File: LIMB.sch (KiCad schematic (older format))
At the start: 67 parts, among them J2 MICROSD, J6 DEBUG, M1 FAN-4PIN, Q12 FK3303010L, Q13 FK3303010L, Q20 FK3303010L, Q21 FK3303010L, Q3 IRLML6402, U10 MAX3232PW, U11 NUF2042XV6, U12 NUF2042XV6, U13 NUF2042XV6, U14 NUF2042XV6, U15 2048mV, U9 NUF2042XV6

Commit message: Squiggles! Silk!
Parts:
- renumbered C134 to C201, C135 to C202, C136 to C203, C137 to C204, C131 to C205, C138 to C206, C139 to C207, C140 to C208, C141 to C209, C9 to C210, C130 to C211, C129 to C212, C127 to C213, C128 to C214, C125 to C215, C126 to C216, J6 to J201, J2 to J202, M1 to M201, Q3 to Q201, Q13 to Q202, Q21 to Q203, Q12 to Q204, Q20 to Q205, R131 to R201, R17 to R202, R102 to R203, R103 to R204, R104 to R205, R116 to R206, R139 to R207, R140 to R208, R142 to R209, R144 to R210, R141 to R211, R143 to R212, R56 to R213, R120 to R214, R121 to R215, R122 to R216, R123 to R217, R124 to R218, R125 to R219, R95 to R220, R126 to R221, R4 to R222, R94 to R223, R93 to R224, R92 to R225, R9 to R226, R86 to R227, R97 to R228, R3 to R229, R87 to R230, R8 to R231, R55 to R232, R96 to R233, U15 to U201, U12 to U202, U13 to U203, U14 to U204, U11 to U205, U10 to U206, U9 to U207, W6 to W201, W7 to W202

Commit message: Initial BOM
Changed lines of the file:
@@
 Wire Wire Line
 	5800 8700 5700 8700
+Wire Notes Line
+	2350 11000 2350 0
+Wire Notes Line
+	4350 0    4350 11000
+Wire Notes Line
+	6300 11000 6300 0
+Wire Notes Line
+	8300 0    8300 11000
+Wire Notes Line
+	10250 11000 10250 0
+Wire Notes Line
+	12200 0    12200 11000
+Wire Notes Line
+	14150 11000 14150 0
+Wire Notes Line
+	16150 0    16150 11000
+Wire Notes Line
+	0    2400 17000 2400
+Wire Notes Line
+	0    4350 17000 4350
+Wire Notes Line
+	17000 6300 -50  6300
+Wire Notes Line
+	0    8300 17000 8300
+Wire Notes Line
+	17000 10250 0    10250
 $EndSCHEMATC

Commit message: Final BOM
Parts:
- added R234: 51, IPC7351-Nominal:RESC1005X40, symbol R-0402
- C212: value 100n -> 1u; BOM CAP MLCC 100n ≥X5R 25V 10% [0402] -> CAP MLCC 1u 6.3V [0402]
- R201, R203, R204, R205, R206, R220, R229: value 5k1 -> 4k3; BOM RES SMD 5k1 1% [0402] -> RES SMD 4k3 [0402]
- R202: value 24 -> 51; BOM RES SMD 24 1% [0402] -> RES SMD 51 1% [0402]
- R207, R208, R210, R211, R212: value 5k1 -> 4k3; BOM RES SMD 5k1 1% [0402] -> RES SMD 4k3 1% [0402]
- R209: value 51k -> 22k6; BOM RES SMD 51k 1% [0402] -> RES SMD 22k6 1% [0402]
- R226, R227, R228, R231, R232, R233: value 3k9 -> 4k3; BOM RES SMD 3k9 1% [0402] -> RES SMD 4k3 1% [0402]
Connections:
- net FPGA_DATA: now also R234.2
- net MOSI: now also R234.1
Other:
- moved on the sheet: R202, R229

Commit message: Finish most redone routing
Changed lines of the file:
@@
 Wire Wire Line
 	5800 8700 5700 8700
-Wire Notes Line
-	2350 11000 2350 0
-Wire Notes Line
-	4350 0    4350 11000
-Wire Notes Line
-	6300 11000 6300 0
-Wire Notes Line
-	8300 0    8300 11000
-Wire Notes Line
-	10250 11000 10250 0
-Wire Notes Line
-	12200 0    12200 11000
-Wire Notes Line
-	14150 11000 14150 0
-Wire Notes Line
-	16150 0    16150 11000
-Wire Notes Line
-	0    2400 17000 2400
-Wire Notes Line
-	0    4350 17000 4350
-Wire Notes Line
-	17000 6300 -50  6300
-Wire Notes Line
-	0    8300 17000 8300
-Wire Notes Line
-	17000 10250 0    10250
 $Comp
 L R-0402 R234

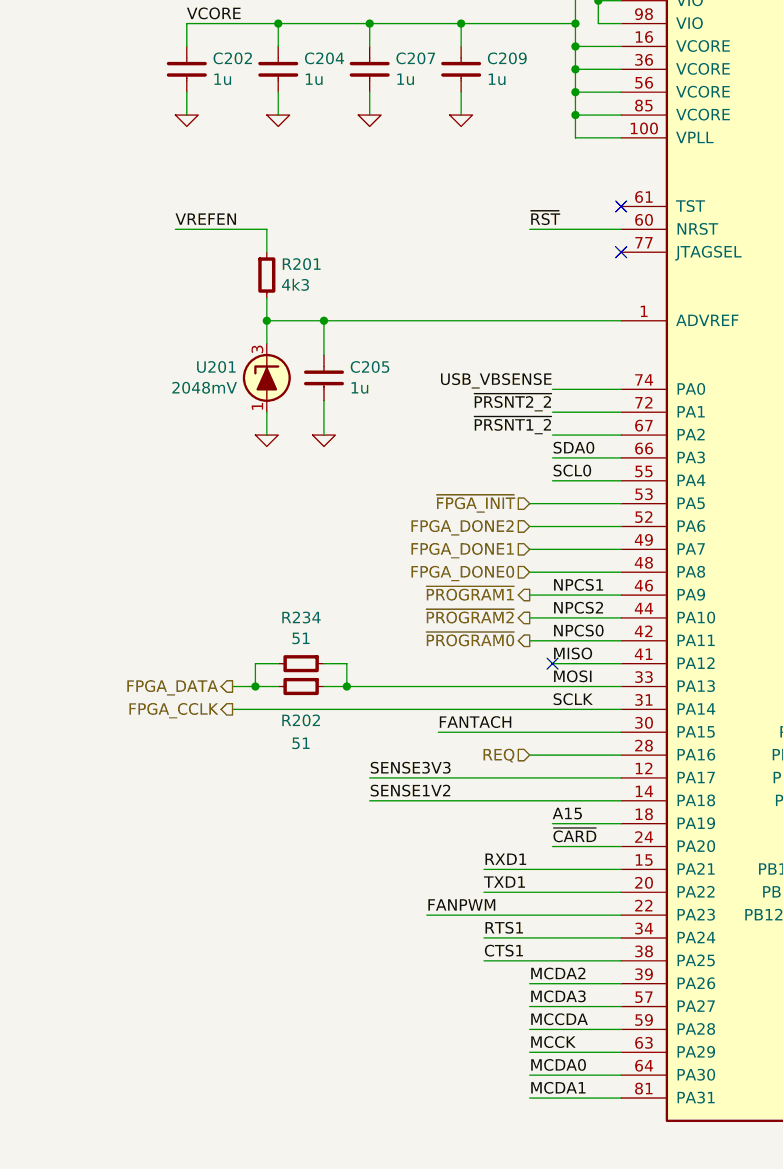
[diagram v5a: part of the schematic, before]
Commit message: Add some test points
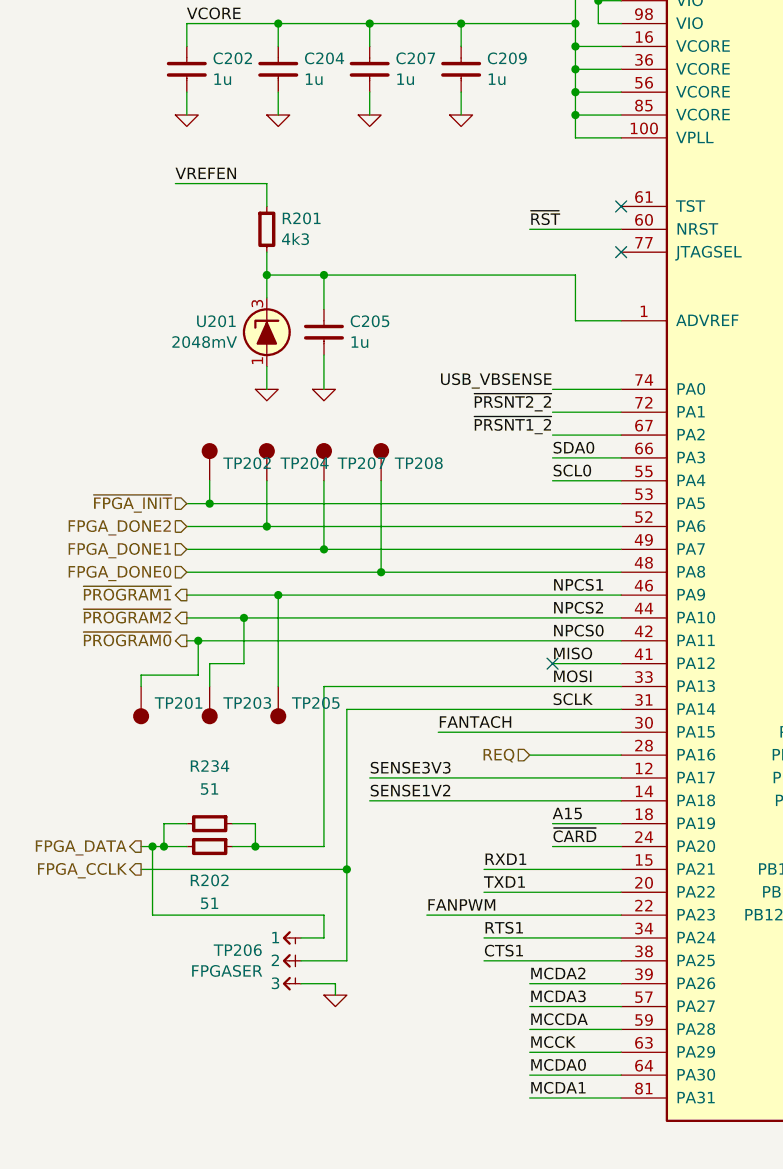
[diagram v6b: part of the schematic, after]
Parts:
- added TP201, TP202, TP203, TP204, TP205, TP207, TP208: TESTPOINT, conn-test:TEST-SMD-SMALL, symbol TESTPOINT
- added TP206: FPGASER, conn-100mil:CONN-100MIL-M-1x3, symbol CONN-100MIL-M-1x3
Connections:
- net FPGA_CCLK: now also TP206.2
- net FPGA_DATA: now also TP206.1
- net FPGA_DONE0: now also TP208.1
- net FPGA_DONE1: now also TP207.1
- net FPGA_DONE2: now also TP204.1
- net GND: now also TP206.3
- net ~FPGA_INIT: now also TP202.1
- net ~PROGRAM0: now also TP201.1
- net ~PROGRAM1: now also TP205.1
- net ~PROGRAM2: now also TP203.1
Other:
- moved on the sheet: C205, R201, R202, R234, U201

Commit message: Fix more shit for to pass ERC
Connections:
- net ~SDRAM_RST: now reaches LIMB1.93 (PB13)
- no-connect marks 14 -> 13
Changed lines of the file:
@@
 USB_D-
 $Comp
-L GND #PWR213
+L GND #PWR031
 U 1 1 577EAB82
 P 4400 6700
-F 0 "#PWR213" H 4400 6700 30  0001 C CNN
+F 0 "#PWR031" H 4400 6700 30  0001 C CNN
 F 1 "GND" H 4400 6630 30  0001 C CNN
 F 2 "" H 4400 6700 60  0000 C CNN
@@
 $EndComp
 $Comp
-L GND #PWR223
+L GND #PWR032
 U 1 1 577EDCE7
 P 10400 4700
-F 0 "#PWR223" H 10400 4700 30  0001 C CNN
+F 0 "#PWR032" H 10400 4700 30  0001 C CNN
 F 1 "GND" H 10400 4630 30  0001 C CNN
 F 2 "" H 10400 4700 60  0000 C CNN
@@
 MCDA3
 $Comp
-L GND #PWR222
+L GND #PWR033
 U 1 1 577EDF0A
 P 10400 4000
-F 0 "#PWR222" H 10400 4000 30  0001 C CNN
+F 0 "#PWR033" H 10400 4000 30  0001 C CNN
 F 1 "GND" H 10400 3930 30  0001 C CNN
 F 2 "" H 10400 4000 60  0000 C CNN
@@
 P3V3_CARD
 $Comp
-L GND #PWR220
+L GND #PWR034
 U 1 1 577EEC84
 P 9600 4200
-F 0 "#PWR220" H 9600 4200 30  0001 C CNN
+F 0 "#PWR034" H 9600 4200 30  0001 C CNN
 F 1 "GND" H 9600 4130 30  0001 C CNN
 F 2 "" H 9600 4200 60  0000 C CNN
@@
 ~RST
 $Comp
-L GND #PWR212
+L GND #PWR035
 U 1 1 579F6A32
 P 2800 8000
-F 0 "#PWR212" H 2800 8000 30  0001 C CNN
+F 0 "#PWR035" H 2800 8000 30  0001 C CNN
 F 1 "GND" H 2800 7930 30  0001 C CNN
 F 2 "" H 2800 8000 60  0000 C CNN
@@
 $EndComp
 $Comp
-L GND #PWR232
+L GND #PWR036
 U 1 1 57A172F2
 P 14800 1650
-F 0 "#PWR232" H 14800 1650 30  0001 C CNN
+F 0 "#PWR036" H 14800 1650 30  0001 C CNN
 F 1 "GND" H 14800 1580 30  0001 C CNN
 F 2 "" H 14800 1650 60  0000 C CNN
@@
 $EndComp
 $Comp
-L GND #PWR228
+L GND #PWR037
 U 1 1 57A1D8E5
 P 13950 3400
-F 0 "#PWR228" H 13950 3400 30  0001 C CNN
+F 0 "#PWR037" H 13950 3400 30  0001 C CNN
 F 1 "GND" H 13950 3330 30  0001 C CNN
 F 2 "" H 13950 3400 60  0000 C CNN
@@
 $EndComp
 $Comp
-L GND #PWR226
+L GND #PWR038
 U 1 1 57A1DE24
 P 12050 3400
-F 0 "#PWR226" H 12050 3400 30  0001 C CNN
+F 0 "#PWR038" H 12050 3400 30  0001 C CNN
 F 1 "GND" H 12050 3330 30  0001 C CNN
 F 2 "" H 12050 3400 60  0000 C CNN
@@
 $EndComp
 $Comp
-L GND #PWR225
+L GND #PWR039
 U 1 1 57A1E179
 P 11800 3250
-F 0 "#PWR225" H 11800 3250 30  0001 C CNN
+F 0 "#PWR039" H 11800 3250 30  0001 C CNN
 F 1 "GND" H 11800 3180 30  0001 C CNN
 F 2 "" H 11800 3250 60  0000 C CNN
@@
 P3V3_STBY
 $Comp
-L GND #PWR227
+L GND #PWR040
 U 1 1 57A1EEA9
 P 12300 4200
-F 0 "#PWR227" H 12300 4200 30  0001 C CNN
+F 0 "#PWR040" H 12300 4200 30  0001 C CNN
 F 1 "GND" H 12300 4130 30  0001 C CNN
 F 2 "" H 12300 4200 60  0000 C CNN
@@
 $EndComp
 $Comp
-L GND #PWR234
+L GND #PWR041
 U 1 1 57A22C9D
 P 14900 4450
-F 0 "#PWR234" H 14900 4450 30  0001 C CNN
+F 0 "#PWR041" H 14900 4450 30  0001 C CNN
 F 1 "GND" H 14900 4380 30  0001 C CNN
 F 2 "" H 14900 4450 60  0000 C CNN
@@
 $EndComp
 $Comp
-L GND #PWR231
+L GND #PWR042
 U 1 1 57A22E58
 P 14600 4450
-F 0 "#PWR231" H 14600 4450 30  0001 C CNN
+F 0 "#PWR042" H 14600 4450 30  0001 C CNN
 F 1 "GND" H 14600 4380 30  0001 C CNN
 F 2 "" H 14600 4450 60  0000 C CNN
@@
 $EndComp
 $Comp
-L GND #PWR230
+L GND #PWR043
 U 1 1 57A22FB0
 P 14300 4450
-F 0 "#PWR230" H 14300 4450 30  0001 C CNN
+F 0 "#PWR043" H 14300 4450 30  0001 C CNN
 F 1 "GND" H 14300 4380 30  0001 C CNN
 F 2 "" H 14300 4450 60  0000 C CNN
@@
 $EndComp
 $Comp
-L GND #PWR229
+L GND #PWR044
 U 1 1 57A23109
 P 14000 4450
-F 0 "#PWR229" H 14000 4450 30  0001 C CNN
+F 0 "#PWR044" H 14000 4450 30  0001 C CNN
 F 1 "GND" H 14000 4380 30  0001 C CNN
 F 2 "" H 14000 4450 60  0000 C CNN
@@
 $EndComp
 $Comp
-L GND #PWR221
+L GND #PWR045
 U 1 1 57A3FEDE
 P 10000 2100
-F 0 "#PWR221" H 10000 2100 30  0001 C CNN
+F 0 "#PWR045" H 10000 2100 30  0001 C CNN
 F 1 "GND" H 10000 2030 30  0001 C CNN
 F 2 "" H 10000 2100 60  0000 C CNN
@@
 $EndComp
 $Comp
-L GND #PWR219
+L GND #PWR046
 U 1 1 57A41BDC
 P 9200 2400
-F 0 "#PWR219" H 9200 2400 30  0001 C CNN
+F 0 "#PWR046" H 9200 2400 30  0001 C CNN
 F 1 "GND" H 9200 2330 30  0001 C CNN
 F 2 "" H 9200 2400 60  0000 C CNN
@@
 $EndComp
 $Comp
-L GND #PWR224
+L GND #PWR047
 U 1 1 57A49C3C
 P 10500 1750
-F 0 "#PWR224" H 10500 1750 30  0001 C CNN
+F 0 "#PWR047" H 10500 1750 30  0001 C CNN
 F 1 "GND" H 10500 1680 30  0001 C CNN
 F 2 "" H 10500 1750 60  0000 C CNN
@@
 XUSB_D+
 $Comp
-L GND #PWR233
+L GND #PWR048
 U 1 1 57AA14DB
 P 14800 2400
-F 0 "#PWR233" H 14800 2400 30  0001 C CNN
+F 0 "#PWR048" H 14800 2400 30  0001 C CNN
 F 1 "GND" H 14800 2330 30  0001 C CNN
 F 2 "" H 14800 2400 60  0000 C CNN
@@
 P3V3_CARD
 $Comp
-L GND #PWR216
+L GND #PWR049
 U 1 1 57A9C7D3
 P 8800 3550
-F 0 "#PWR216" H 8800 3550 30  0001 C CNN
+F 0 "#PWR049" H 8800 3550 30  0001 C CNN
 F 1 "GND" H 8800 3480 30  0001 C CNN
 F 2 "" H 8800 3550 60  0000 C CNN
@@
 $EndComp
 $Comp
-L GND #PWR217
+L GND #PWR050
 U 1 1 57A9C9F3
 P 8800 4650
-F 0 "#PWR217" H 8800 4650 30  0001 C CNN
+F 0 "#PWR050" H 8800 4650 30  0001 C CNN
 F 1 "GND" H 8800 4580 30  0001 C CNN
 F 2 "" H 8800 4650 60  0000 C CNN
@@
 $EndComp
 $Comp
-L GND #PWR218
+L GND #PWR051
 U 1 1 57A9CC0D
 P 8800 5750
-F 0 "#PWR218" H 8800 5750 30  0001 C CNN
+F 0 "#PWR051" H 8800 5750 30  0001 C CNN
 F 1 "GND" H 8800 5680 30  0001 C CNN
 F 2 "" H 8800 5750 60  0000 C CNN
@@
 $EndComp
 $Comp
-L GND #PWR203
+L GND #PWR052
 U 1 1 57AAC080
 P 1550 3500
-F 0 "#PWR203" H 1550 3500 30  0001 C CNN
+F 0 "#PWR052" H 1550 3500 30  0001 C CNN
 F 1 "GND" H 1550 3430 30  0001 C CNN
 F 2 "" H 1550 3500 60  0000 C CNN
@@
 $EndComp
 $Comp
-L GND #PWR206
+L GND #PWR053
 U 1 1 57AB076E
 P 1800 3500
-F 0 "#PWR206" H 1800 3500 30  0001 C CNN
+F 0 "#PWR053" H 1800 3500 30  0001 C CNN
 F 1 "GND" H 1800 3430 30  0001 C CNN
 F 2 "" H 1800 3500 60  0000 C CNN
@@
 $EndComp
 $Comp
-L GND #PWR202
+L GND #PWR054
 U 1 1 57AFC6F6
 P 1200 2300
-F 0 "#PWR202" H 1200 2300 30  0001 C CNN
+F 0 "#PWR054" H 1200 2300 30  0001 C CNN
 F 1 "GND" H 1200 2230 30  0001 C CNN
 F 2 "" H 1200 2300 60  0000 C CNN
@@
 $EndComp
 $Comp
-L GND #PWR205
+L GND #PWR055
 U 1 1 57AFC985
 P 1600 2300
-F 0 "#PWR205" H 1600 2300 30  0001 C CNN
+F 0 "#PWR055" H 1600 2300 30  0001 C CNN
 F 1 "GND" H 1600 2230 30  0001 C CNN
 F 2 "" H 1600 2300 60  0000 C CNN
@@
 $EndComp
 $Comp
-L GND #PWR209
+L GND #PWR056
 U 1 1 57AFCC0E
 P 2000 2300
-F 0 "#PWR209" H 2000 2300 30  0001 C CNN
+F 0 "#PWR056" H 2000 2300 30  0001 C CNN
 F 1 "GND" H 2000 2230 30  0001 C CNN
 F 2 "" H 2000 2300 60  0000 C CNN
@@
 $EndComp
 $Comp
-L GND #PWR211
+L GND #PWR057
 U 1 1 57AFCE98
 P 2400 2300
-F 0 "#PWR211" H 2400 2300 30  0001 C CNN
+F 0 "#PWR057" H 2400 2300 30  0001 C CNN
 F 1 "GND" H 2400 2230 30  0001 C CNN
 F 2 "" H 2400 2300 60  0000 C CNN
@@
 $EndComp
 $Comp
-L GND #PWR210
+L GND #PWR058
 U 1 1 57AFD588
 P 2400 1700
-F 0 "#PWR210" H 2400 1700 30  0001 C CNN
+F 0 "#PWR058" H 2400 1700 30  0001 C CNN
 F 1 "GND" H 2400 1630 30  0001 C CNN
 F 2 "" H 2400 1700 60  0000 C CNN
@@
 $EndComp
 $Comp
-L GND #PWR208
+L GND #PWR059
 U 1 1 57AFD64A
 P 2000 1700
-F 0 "#PWR208" H 2000 1700 30  0001 C CNN
+F 0 "#PWR059" H 2000 1700 30  0001 C CNN
 F 1 "GND" H 2000 1630 30  0001 C CNN
 F 2 "" H 2000 1700 60  0000 C CNN
@@
 $EndComp
 $Comp
-L GND #PWR204
+L GND #PWR060
 U 1 1 57AFD70C
 P 1600 1700
-F 0 "#PWR204" H 1600 1700 30  0001 C CNN
+F 0 "#PWR060" H 1600 1700 30  0001 C CNN
 F 1 "GND" H 1600 1630 30  0001 C CNN
 F 2 "" H 1600 1700 60  0000 C CNN
@@
 $EndComp
 $Comp
-L GND #PWR201
+L GND #PWR061
 U 1 1 57AFD7CE
 P 1200 1700
-F 0 "#PWR201" H 1200 1700 30  0001 C CNN
+F 0 "#PWR061" H 1200 1700 30  0001 C CNN
 F 1 "GND" H 1200 1630 30  0001 C CNN
 F 2 "" H 1200 1700 60  0000 C CNN
@@
 $EndComp
 $Comp
-L GND #PWR214
+L GND #PWR062
 U 1 1 57AD7374
 P 6100 7650
-F 0 "#PWR214" H 6100 7650 30  0001 C CNN
+F 0 "#PWR062" H 6100 7650 30  0001 C CNN
 F 1 "GND" H 6100 7580 30  0001 C CNN
 F 2 "" H 6100 7650 60  0000 C CNN
@@
 $EndComp
 $Comp
-L GND #PWR215
+L GND #PWR063
 U 1 1 57ADB7CD
 P 6100 8500
-F 0 "#PWR215" H 6100 8500 30  0001 C CNN
+F 0 "#PWR063" H 6100 8500 30  0001 C CNN
 F 1 "GND" H 6100 8430 30  0001 C CNN
 F 2 "" H 6100 8500 60  0000 C CNN
@@
 NoConn ~ 4400 5400
 NoConn ~ 4300 5800
-NoConn ~ 4300 5900
 NoConn ~ 4300 6000
 Wire Wire Line
@@
 Connection ~ 1900 5600
 $Comp
-L GND #PWR207
+L GND #PWR064
 U 1 1 57C88932
 P 1850 6150
-F 0 "#PWR207" H 1850 6150 30  0001 C CNN
+F 0 "#PWR064" H 1850 6150 30  0001 C CNN
 F 1 "GND" H 1850 6080 30  0001 C CNN
 F 2 "" H 1850 6150 60  0000 C CNN
@@
 	1800 5800 1800 5900
 Connection ~ 1050 5500
+Text HLabel 15300 9300 2    50   Output ~ 0
+~SDRAM_RST
+Wire Wire Line
+	15300 9300 11800 9300
+Text Label 11800 9300 0    50   ~ 0
+~SDRAM_RST
+Text Label 4400 5900 0    50   ~ 0
+~SDRAM_RST
+Wire Wire Line
+	4300 5900 4400 5900
 $EndSCHEMATC
